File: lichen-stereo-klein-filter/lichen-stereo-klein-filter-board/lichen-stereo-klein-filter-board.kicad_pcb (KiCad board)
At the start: 2 copper layers, 29 x 108 mm, 85 parts, among them J8 Conn_02x07_Top_Bottom, U2 TL074, U3 TL074, U4 TL074, U5 TL074, U6 TL072

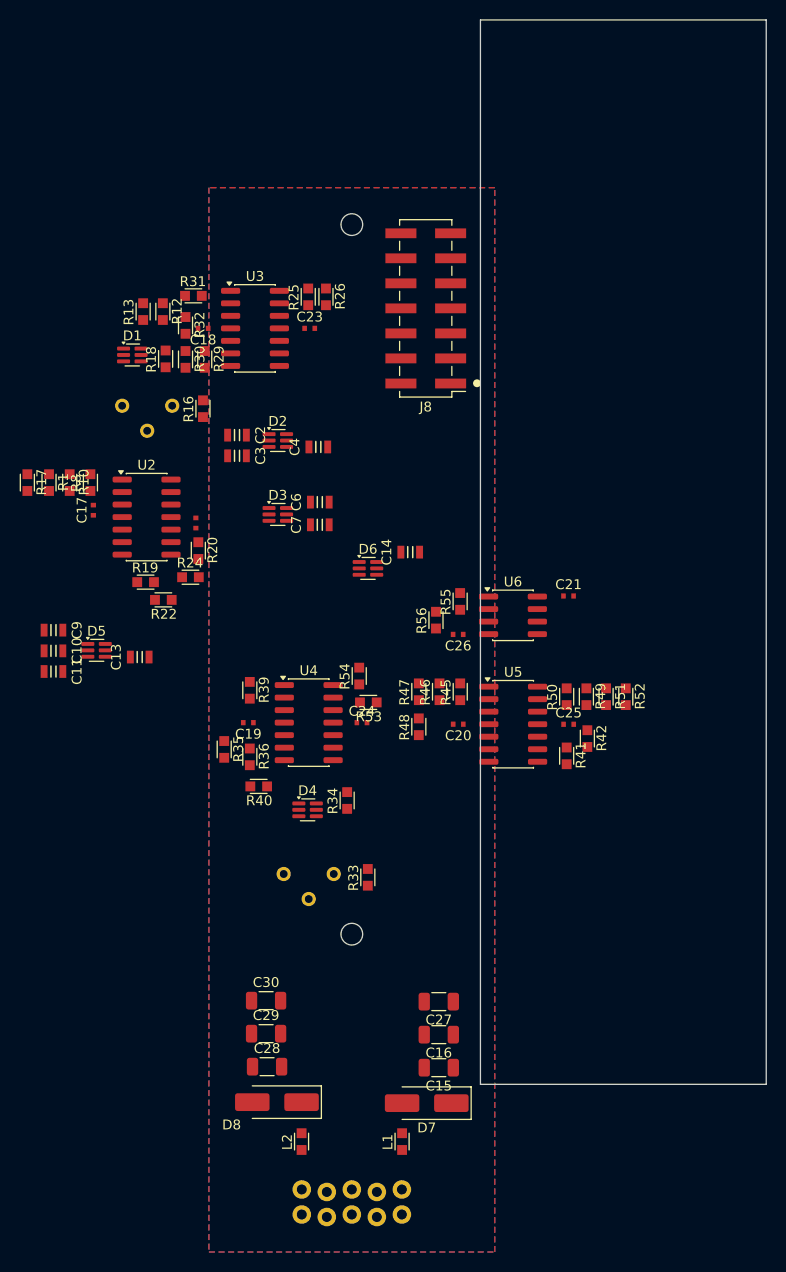
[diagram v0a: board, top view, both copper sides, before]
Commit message: feat: Updates Crustose, Cladonia and YouMe Transformer. Adds Stereo Latencies.
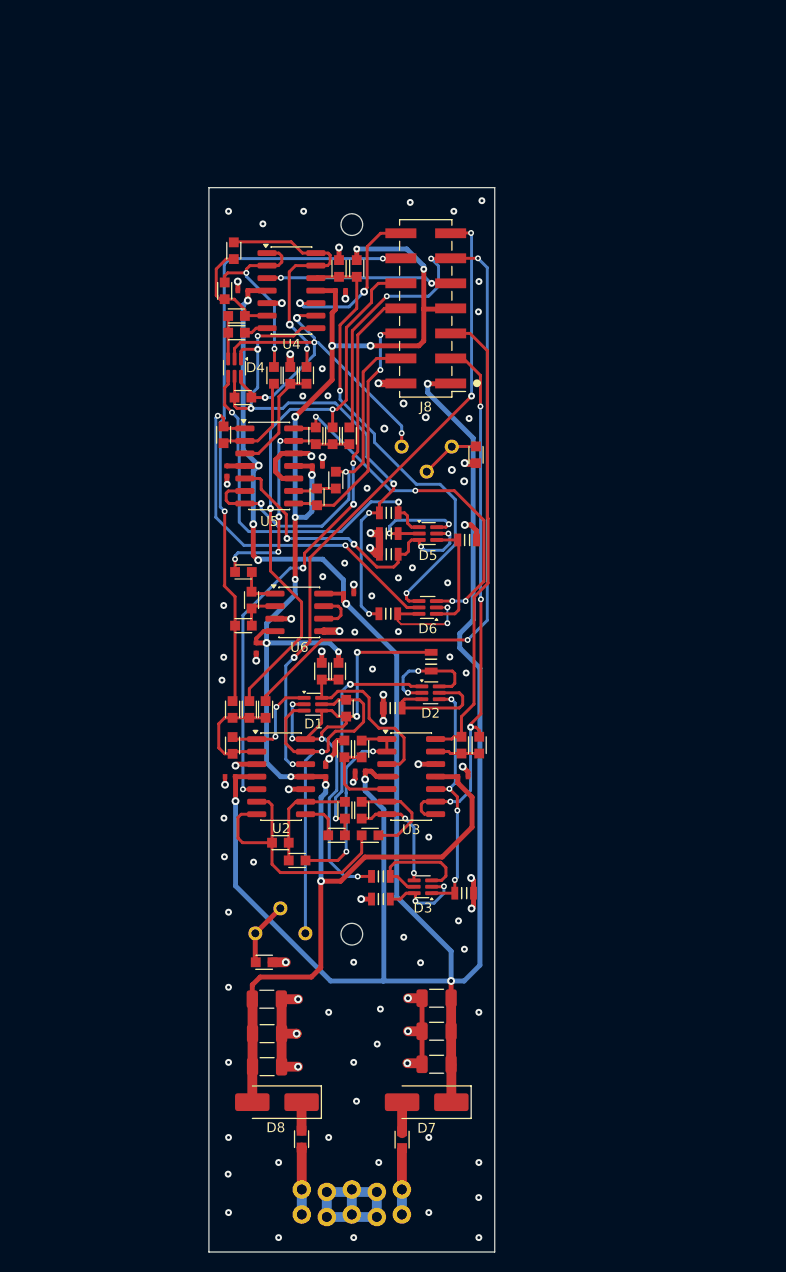
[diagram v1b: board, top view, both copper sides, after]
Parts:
- J8: value Conn_02x07_Top_Bottom -> 02x07 Pins
- moved RV5 56.7 mm to (110.3, 185.9), turned to 0 degrees
- moved R16 56.5 mm to (106.1, 188.8), turned to 180 degrees
- moved R30 51.8 mm to (116.8, 176.0), turned to 180 degrees
- moved R31 49.0 mm to (116.0, 167.2), turned to 90 degrees
- moved R29 48.4 mm to (116.0, 173.4)
- moved U3 48.2 mm to (121.0, 170.0)
- moved C23 48.1 mm to (126.3, 170.0)
- moved R25 48.1 mm to (126.1, 166.8)
- moved R26 48.1 mm to (127.9, 166.8)
- moved C18 47.7 mm to (115.8, 169.5)
- moved C4 47.6 mm to (126.4, 181.8)
- moved R35 46.5 mm to (102.1, 120.7)
- moved R40 46.1 mm to (103.3, 125.0)
- moved R32 45.9 mm to (114.2, 167.2)
- moved D4 45.5 mm to (103.1, 128.5), turned to -90 degrees
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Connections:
- net AUDIO_OUT_UNFILTERED_L renamed AUDIO_OUT_DC_COUPLED_L
- net AUDIO_OUT_UNFILTERED_R renamed AUDIO_OUT_DC_COUPLED_R
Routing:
- net +12V: track 0.00 -> 237.0 mm, vias 0 -> 9
- net -12V: track 0.00 -> 173.6 mm, vias 0 -> 13
- net GND: track 0.00 -> 92.7 mm, vias 0 -> 100
- net CUTOFF_CV_OFFSET: track 0.00 -> 91.7 mm, vias 0 -> 4
- net RESONANCE_ATTEN_L: track 0.00 -> 65.6 mm, vias 0 -> 4
- net SKEW_CV_MIXED: track 0.00 -> 63.4 mm, vias 0 -> 2
- net AUDIO_IN_SCALED_L: track 0.00 -> 58.6 mm, vias 0 -> 4
- net CUTOFF_CV_IN: track 0.00 -> 57.3 mm, vias 0 -> 2
- net /R_RESONANCE: track 0.00 -> 57.2 mm, vias 0 -> 6
- net LADDER_OUT_L: track 0.00 -> 55.8 mm, vias 0 -> 4
- net /L_RESONANCE: track 0.00 -> 51.8 mm, vias 0 -> 6
- net AUDIO_OUT_DC_COUPLED_L: track 0.00 -> 47.5 mm
- net Net-(D6C-K): track 0.00 -> 47.2 mm, vias 0 -> 2
- net Net-(D4A-K): track 0.00 -> 41.2 mm, vias 0 -> 4
- net Net-(D1B-K): track 0.00 -> 40.9 mm, vias 0 -> 1
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- added copper zone on In1.Cu, net GND
- added copper zone on In2.Cu, net GND
- removed copper zone on B.Cu, net GND
- removed copper zone on F.Cu, net GND
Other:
- copper layers 2 -> 4
- board text added: "Cladonia filter board v1.0 © 2026, Colin Clark Thank you to Moritz Klein and Erica Synths"
- board text added: "Lichen Cladonia"
- board text added: "Power header & trimmers this side"
